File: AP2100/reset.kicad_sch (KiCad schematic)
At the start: 111 parts, among them IC4 MIC2774N-29YM5-TR, IC5 PCF2129T_2,518, J3 Conn_ARM_JTAG_SWD_10, J4 RJ45, SW1 RESET, U10 SA56004EDP,118, U11 SP3232EBEY-L/TR, U12 74LVC1G08, U13 74LVC1G08, U14 74LVC1G07, U15 74LVC1G07, U16 74LVC1G08, U17 74LVC1G07, U18 ATECC608A-MAHDA, U19 74LVC1G08, U20 74LVC1G07, U7 LS1043ASE7KQB-Layerscape, U9 74LVC2G08

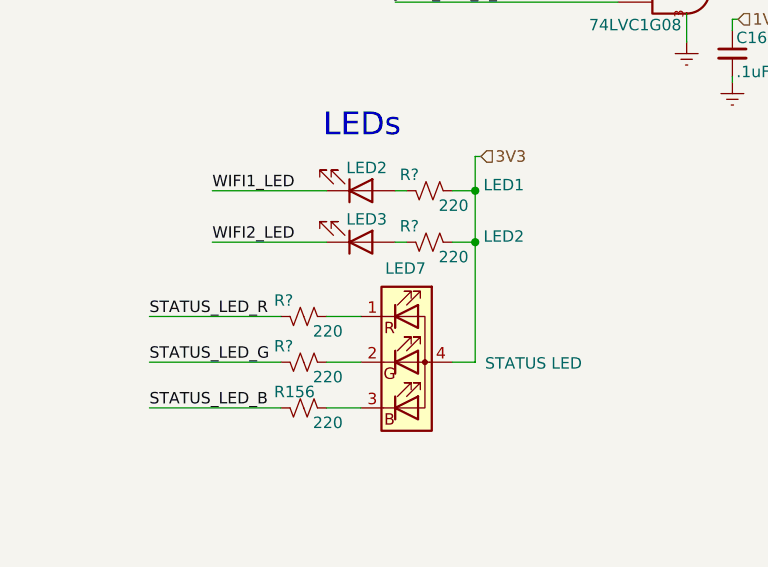
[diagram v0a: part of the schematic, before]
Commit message: Added antenna mounting holes
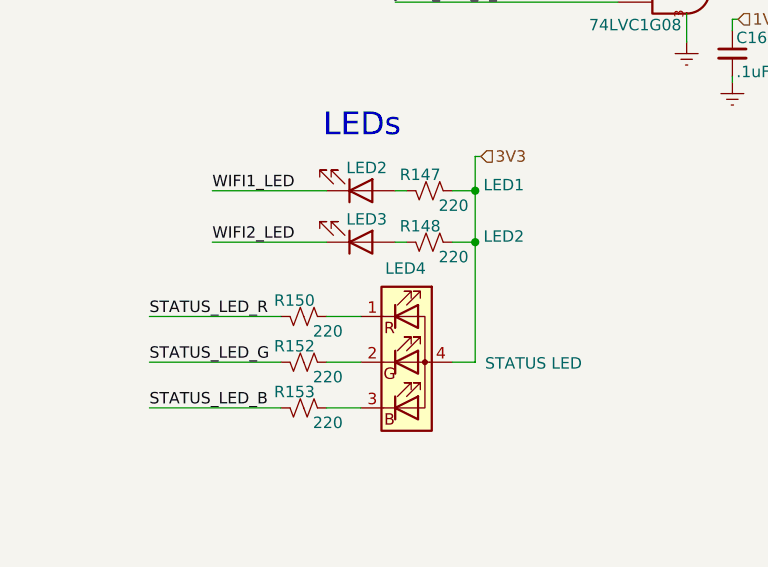
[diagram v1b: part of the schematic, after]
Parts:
- gave numbers to parts that had none: 4
- renumbered LED7 to LED4, R156 to R153
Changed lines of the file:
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@@
   (symbol (lib_id "Device:R_Small_US") (at 43.815 241.935 270) (mirror x) (unit 1)
     (in_bom yes) (on_board yes)
-    (property "Reference" "R?" (id 0) (at 40.513 240.157 90)
+    (property "Reference" "R150" (id 0) (at 40.513 240.157 90)
       (effects (font (size 1.27 1.27)) (justify left))
     )
@@
   (symbol (lib_id "Device:R_Small_US") (at 43.815 247.015 270) (mirror x) (unit 1)
     (in_bom yes) (on_board yes)
-    (property "Reference" "R?" (id 0) (at 40.513 245.237 90)
+    (property "Reference" "R152" (id 0) (at 40.513 245.237 90)
       (effects (font (size 1.27 1.27)) (justify left))
     )
@@
   (symbol (lib_id "Device:R_Small_US") (at 43.815 252.095 270) (mirror x) (unit 1)
     (in_bom yes) (on_board yes)
-    (property "Reference" "R156" (id 0) (at 40.513 250.317 90)
+    (property "Reference" "R153" (id 0) (at 40.513 250.317 90)
       (effects (font (size 1.27 1.27)) (justify left))
     )
@@
   (symbol (lib_id "Device:R_Small_US") (at 57.785 227.965 270) (mirror x) (unit 1)
     (in_bom yes) (on_board yes)
-    (property "Reference" "R?" (id 0) (at 54.483 226.187 90)
+    (property "Reference" "R147" (id 0) (at 54.483 226.187 90)
       (effects (font (size 1.27 1.27)) (justify left))
     )
@@
   (symbol (lib_id "Device:R_Small_US") (at 57.785 233.68 270) (mirror x) (unit 1)
     (in_bom yes) (on_board yes)
-    (property "Reference" "R?" (id 0) (at 54.483 231.902 90)
+    (property "Reference" "R148" (id 0) (at 54.483 231.902 90)
       (effects (font (size 1.27 1.27)) (justify left))
     )
@@
   (symbol (lib_id "Device:LED_RGBA") (at 55.245 247.015 0) (unit 1)
     (in_bom yes) (on_board yes)
-    (property "Reference" "LED7" (id 0) (at 55.118 236.601 0))
+    (property "Reference" "LED4" (id 0) (at 55.118 236.601 0))
     (property "Value" "STATUS LED" (id 1) (at 69.342 247.142 0))
     (property "Footprint" "LED_SMD:LED_Cree-PLCC4_2x2mm_CW" (id 2) (at 55.245 248.285 0)

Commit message: More cleanups
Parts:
- added R102, R103: 1K, Resistor_SMD:R_0402_1005Metric, symbol Device:R_Small_US
- added R110: 4.7K, Resistor_SMD:R_0402_1005Metric, symbol Device:R_Small_US
- R108: renamed from R105; value 1K -> 4.7K; PartsBoxID 0402-1K-1% -> 0402-4.7K-1%
- renumbered R134 to R100, R133 to R101, R101 to R104, R102 to R105, R103 to R106, R104 to R107, R106 to R109, R107 to R111, R108 to R112, R109 to R113, R110 to R114, R111 to R115, R112 to R116, R113 to R117, R114 to R118, R115 to R119, R116 to R120, R117 to R121, R118 to R122, R119 to R123, R120 to R124, R121 to R125, R122 to R126, R123 to R127, R124 to R128, R125 to R129, R126 to R130, R127 to R131, R128 to R132, R129 to R133, R130 to R134, R131 to R135, R132 to R136, R135 to R137, R136 to R138, R137 to R139, R138 to R140, R139 to R141, R140 to R142, R141 to R143, R142 to R144, R143 to R145, R144 to R146, R145 to R147, R146 to R148, R147 to R149, R148 to R150, R149 to R151, R150 to R152, R151 to R153, R152 to R154, R153 to R155, R89 to R88, R90 to R89, R91 to R90, R92 to R91, R93 to R92, R94 to R93, R95 to R94, R96 to R95, R97 to R96, R98 to R97, R99 to R98, R100 to R99
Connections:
- net 3V3: now also R102.2, R103.2
- net I2C1_SCL: now also R101.1
- net I2C1_SDA: now also R100.1
- net I2C2_SCL: now also R103.1
- net I2C2_SDA: now also R102.1
- net VDD_LP: now also R110.1; no longer U7.G19 (~TA_BB_TMP_DETECT~)
- net at IC5.4 (SDA/~CE), R142.2: no longer R100.1
- net at IC5.1 (SCL), R139.2: no longer R101.1
- new net: R110.2, U7.G19 (~TA_BB_TMP_DETECT~)
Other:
- moved on the sheet: C149, C151, R100, R101, R104, R105, R106, R107, R109, R111, R112, R113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

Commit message: Not sure
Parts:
- IC5: PartsBoxID (none) -> PCF2129T_2,518
- U10: PartsBoxID (none) -> SA56004EDP,118
- U11: value SP3232EBEY-L/TR -> SP3232EBEY-L/TR; PartsBoxID (none) -> SP3232EBEY-L/TR
- U12, U13, U16, U19: PartsBoxID (none) -> 74LVC1G08
- U14, U15, U17, U20: PartsBoxID (none) -> 74LVC1G07
- U18: PartsBoxID (none) -> ATECC608A-MAHDA
- U7: value LS1043ASE7KQB-Layerscape -> LS1043ASE7xxx; PartsBoxID (none) -> LS1043ASE7
- U9: PartsBoxID (none) -> 74LVC2G08
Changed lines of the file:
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@@
   (junction (at 376.555 177.8) (diameter 0.9144) (color 0 0 0 0))
   (no_connect (at 106.68 109.22))
-  (no_connect (at 238.76 71.12))
   (no_connect (at 217.805 177.165))
+  (no_connect (at 217.805 184.785))
   (no_connect (at 238.76 55.88))
+  (no_connect (at 238.76 71.12))
   (no_connect (at 250.825 179.705))
-  (no_connect (at 217.805 184.785))
   (wire (pts (xy 26.67 241.935) (xy 41.275 241.935))
     (stroke (width 0) (type solid) (color 0 0 0 0))
@@
     (stroke (width 0) (type solid) (color 0 0 0 0))
   )
-  (wire (pts (xy 317.5 57.15) (xy 317.5 59.69))
-    (stroke (width 0) (type solid) (color 0 0 0 0))
-  )
-  (wire (pts (xy 317.5 59.69) (xy 317.5 60.325))
+  (wire (pts (xy 317.5 57.15) (xy 317.5 60.325))
     (stroke (width 0) (type solid) (color 0 0 0 0))
   )
@@
     (stroke (width 0) (type solid) (color 0 0 0 0))
   )
-  (wire (pts (xy 340.995 57.15) (xy 340.995 59.69))
-    (stroke (width 0) (type solid) (color 0 0 0 0))
-  )
-  (wire (pts (xy 340.995 59.69) (xy 340.995 60.325))
+  (wire (pts (xy 340.995 57.15) (xy 340.995 60.325))
     (stroke (width 0) (type solid) (color 0 0 0 0))
   )
@@
       (effects (font (size 1.27 1.27)) hide)
     )
+    (property "PartsBoxID" "74LVC2G08" (id 4) (at 72.39 43.18 0)
+      (effects (font (size 1.27 1.27)) hide)
+    )
   )
   (symbol (lib_name "Scott:74LVC1G08_2") (lib_id "Scott:74LVC1G08") (at 86.36 205.74 0) (unit 1)
@@
       (effects (font (size 1.27 1.27)) hide)
     )
+    (property "PartsBoxID" "74LVC1G08" (id 4) (at 86.36 205.74 0)
+      (effects (font (size 1.27 1.27)) hide)
+    )
   )
   (symbol (lib_name "Scott:74LVC1G08_1") (lib_id "Scott:74LVC1G08") (at 101.6 189.865 0) (unit 1)
@@
       (effects (font (size 1.27 1.27)) hide)
     )
+    (property "PartsBoxID" "74LVC1G08" (id 4) (at 101.6 189.865 0)
+      (effects (font (size 1.27 1.27)) hide)
+    )
   )
   (symbol (lib_name "Scott:74LVC1G07_1") (lib_id "Scott:74LVC1G07") (at 146.05 205.74 0) (unit 1)
@@
       (effects (font (size 1.27 1.27)) hide)
     )
+    (property "PartsBoxID" "74LVC1G07" (id 4) (at 146.05 205.74 0)
+      (effects (font (size 1.27 1.27)) hide)
+    )
   )
   (symbol (lib_name "Scott:74LVC1G07_2") (lib_id "Scott:74LVC1G07") (at 146.05 220.98 0) (unit 1)
@@
       (effects (font (size 1.27 1.27)) hide)
     )
+    (property "PartsBoxID" "74LVC1G07" (id 4) (at 146.05 220.98 0)
+      (effects (font (size 1.27 1.27)) hide)
+    )
   )
   (symbol (lib_name "Scott:74LVC1G08_3") (lib_id "Scott:74LVC1G08") (at 150.495 239.395 0) (unit 1)
@@
       (effects (font (size 1.27 1.27)) hide)
     )
+    (property "PartsBoxID" "74LVC1G08" (id 4) (at 150.495 239.395 0)
+      (effects (font (size 1.27 1.27)) hide)
+    )
   )
   (symbol (lib_id "Scott:74LVC1G08") (at 150.495 259.08 0) (unit 1)
@@
       (effects (font (size 1.27 1.27)) hide)
     )
+    (property "PartsBoxID" "74LVC1G08" (id 4) (at 150.495 259.08 0)
+      (effects (font (size 1.27 1.27)) hide)
+    )
   )
   (symbol (lib_name "Scott:74LVC1G07_3") (lib_id "Scott:74LVC1G07") (at 174.625 239.395 0) (unit 1)
@@
       (effects (font (size 1.27 1.27)) hide)
     )
+    (property "PartsBoxID" "74LVC1G07" (id 4) (at 174.625 239.395 0)
+      (effects (font (size 1.27 1.27)) hide)
+    )
   )
   (symbol (lib_id "Scott:74LVC1G07") (at 174.625 259.08 0) (unit 1)
@@
       (effects (font (size 1.27 1.27)) hide)
     )
+    (property "PartsBoxID" "74LVC1G07" (id 4) (at 174.625 259.08 0)
+      (effects (font (size 1.27 1.27)) hide)
+    )
   )
   (symbol (lib_id "Scott:74LVC2G08") (at 328.295 97.79 0) (unit 2)
@@
       (effects (font (size 1.27 1.27)) hide)
     )
+    (property "PartsBoxID" "74LVC2G08" (id 4) (at 328.295 97.79 0)
+      (effects (font (size 1.27 1.27)) hide)
+    )
   )
   (symbol (lib_id "Device:LED_RGBA") (at 55.245 247.015 0) (unit 1)
@@
       (effects (font (size 1.27 1.27)) hide)
     )
+    (property "PartsBoxID" "ATECC608A-MAHDA" (id 4) (at 259.08 239.395 0)
+      (effects (font (size 1.27 1.27)) hide)
+    )
   )
   (symbol (lib_id "MIC2774L-29YM5-TR:MIC2774L-29YM5-TR") (at 135.89 164.465 0) (mirror y) (unit 1)
@@
       (effects (font (size 1.27 1.27)) (justify left bottom) hide)
     )
+    (property "PartsBoxID" "SA56004EDP,118" (id 4) (at 283.845 96.52 0)
+      (effects (font (size 1.27 1.27)) hide)
+    )
   )
   (symbol (lib_id "Connector:RJ45") (at 389.89 175.26 180) (unit 1)
@@
       (effects (font (size 1.27 1.27)) (justify left) hide)
     )
+    (property "PartsBoxID" "PCF2129T_2,518" (id 4) (at 217.805 172.085 0)
+      (effects (font (size 1.27 1.27)) hide)
+    )
   )
   (symbol (lib_id "Interface_UART:MAX3232") (at 330.835 165.1 0) (unit 1)
     (in_bom yes) (on_board yes)
     (property "Reference" "U11" (id 0) (at 316.865 137.795 0))
-    (property "Value" "SP3232EBEY-L/TR\n" (id 1) (at 320.04 191.77 0))
+    (property "Value" "SP3232EBEY-L/TR" (id 1) (at 320.04 191.77 0))
     (property "Footprint" "Package_SO:TSSOP-16_4.4x5mm_P0.65mm" (id 2) (at 332.105 191.77 0)
       (effects (font (size 1.27 1.27)) (justify left) hide)
@@
       (effects (font (size 1.27 1.27)) hide)
     )
+    (property "PartsBoxID" "SP3232EBEY-L/TR" (id 4) (at 330.835 165.1 0)
+      (effects (font (size 1.27 1.27)) hide)
+    )
   )
   (symbol (lib_id "AP2100-rescue:LS1043ASE7KQB-Layerscape") (at 171.45 80.01 0) (unit 5)
     (in_bom yes) (on_board yes)
     (property "Reference" "U7" (id 0) (at 173.355 25.4 0))
-    (property "Value" "LS1043ASE7KQB-Layerscape" (id 1) (at 173.355 27.94 0))
+    (property "Value" "LS1043ASE7xxx" (id 1) (at 173.355 27.94 0))
     (property "Footprint" "PLS1043ASE7QQA:BGA621C80P25X25_2100X2100X192N" (id 2) (at 171.45 80.01 0)
       (effects (font (size 1.27 1.27)) hide)
@@
       (effects (font (size 1.27 1.27)) hide)
     )
+    (property "PartsBoxID" "LS1043ASE7" (id 4) (at 171.45 80.01 0)
+      (effects (font (size 1.27 1.27)) hide)
+    )

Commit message: More cleanups - fix incorrect serial console pinout Add netclasses
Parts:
- removed R88, R90, R95, R97: DNP 0, Resistor_SMD:R_0402_1005Metric, symbol Device:R_Small_US
- removed R89, R91, R96, R98: 0, Resistor_SMD:R_0402_1005Metric, symbol Device:R_Small_US
- renumbered R108 to R100, R109 to R101, R110 to R102, R111 to R103, R112 to R104, R113 to R105, R114 to R106, R115 to R107, R116 to R108, R117 to R109, R118 to R110, R119 to R111, R120 to R112, R121 to R113, R122 to R114, R123 to R115, R124 to R116, R125 to R117, R126 to R118, R127 to R119, R128 to R120, R129 to R121, R130 to R122, R131 to R123, R132 to R124, R133 to R125, R134 to R126, R135 to R127, R136 to R128, R137 to R129, R138 to R130, R139 to R131, R141 to R132, R140 to R133, R142 to R134, R143 to R135, R144 to R136, R145 to R137, R146 to R138, R147 to R139, R148 to R140, R149 to R141, R150 to R142, R151 to R143, R152 to R144, R153 to R145, R154 to R146, R155 to R147, R92 to R88, R93 to R89, R94 to R90, R99 to R91, R100 to R92, R101 to R93, R102 to R94, R103 to R95, R104 to R96, R105 to R97, R106 to R98, R107 to R99
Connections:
- net CONSOLE_CTS is gone; now on net UART_RTS: U11.10 (T2IN)
- net CONSOLE_RTS is gone; now on net UART_CTS: U11.9 (R2OUT)
- net CONSOLE_RX is gone; now on net UART_RX: U11.12 (R1OUT)
- net CONSOLE_TX is gone; now on net UART_TX: U11.11 (T1IN)
- net at J4.1: now also U11.7 (T2OUT); no longer U11.8 (R2IN)
- net at J4.8: now also U11.8 (R2IN); no longer U11.7 (T2OUT)
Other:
- note added: "Note: I2C Address: 0x4C"
- note added: "Note: I2C Address: 0x51"
- note added: "Note: I2C Address: 0x60"
- company: (none) -> ISis ImageStream Internet Solutions, Inc.
- title: (none) -> AP2100
- moved on the sheet: BT1, C149, C150, C151, C152, C153, C154, C155, C156, C157, C158, C159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

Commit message: More cleanups
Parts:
- BT1: PartsBoxID (none) -> 2032-BH
- LED6: renamed from LED1; PartsBoxID (none) -> 0805-LED-BLUE
- LED7: renamed from LED2; value LED1 -> WIFI1_LED; PartsBoxID (none) -> 0805-LED-GREEN
- LED8: renamed from LED3; value LED2 -> WIFI2_LED; PartsBoxID (none) -> 0805-LED-GREEN
- LED9: renamed from LED4; PartsBoxID (none) -> 2x2-LED-RGB
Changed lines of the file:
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@@
   (junction (at 69.85 111.125) (diameter 0.9144) (color 0 0 0 0))
   (junction (at 74.295 52.705) (diameter 0.9144) (color 0 0 0 0))
+  (junction (at 74.295 159.385) (diameter 0.9144) (color 0 0 0 0))
   (junction (at 75.565 116.205) (diameter 0.9144) (color 0 0 0 0))
-  (junction (at 76.2 159.385) (diameter 0.9144) (color 0 0 0 0))
   (junction (at 92.075 168.275) (diameter 0.9144) (color 0 0 0 0))
   (junction (at 92.075 182.88) (diameter 0.9144) (color 0 0 0 0))
@@
   (junction (at 365.76 154.305) (diameter 0.9144) (color 0 0 0 0))
   (junction (at 381.635 167.005) (diameter 0.9144) (color 0 0 0 0))
-  (no_connect (at 223.52 168.91))
-  (no_connect (at 223.52 176.53))
-  (no_connect (at 244.475 47.625))
   (no_connect (at 244.475 62.865))
+  (no_connect (at 244.475 47.625))
+  (no_connect (at 223.52 176.53))
+  (no_connect (at 223.52 168.91))
   (no_connect (at 112.395 100.965))
   (no_connect (at 256.54 171.45))
@@
     (stroke (width 0) (type solid) (color 0 0 0 0))
   )
-  (wire (pts (xy 73.66 149.86) (xy 78.74 149.86))
+  (wire (pts (xy 71.755 149.86) (xy 78.74 149.86))
     (stroke (width 0) (type solid) (color 0 0 0 0))
   )
-  (wire (pts (xy 73.66 153.035) (xy 78.74 153.035))
+  (wire (pts (xy 71.755 153.035) (xy 78.74 153.035))
     (stroke (width 0) (type solid) (color 0 0 0 0))
   )
-  (wire (pts (xy 73.66 156.21) (xy 78.74 156.21))
+  (wire (pts (xy 71.755 156.21) (xy 78.74 156.21))
     (stroke (width 0) (type solid) (color 0 0 0 0))
   )
-  (wire (pts (xy 73.66 159.385) (xy 76.2 159.385))
+  (wire (pts (xy 71.755 159.385) (xy 74.295 159.385))
     (stroke (width 0) (type solid) (color 0 0 0 0))
   )
@@
     (stroke (width 0) (type solid) (color 0 0 0 0))
   )
-  (wire (pts (xy 75.565 100.965) (xy 75.565 102.235))
+  (wire (pts (xy 74.295 159.385) (xy 74.295 196.215))
     (stroke (width 0) (type solid) (color 0 0 0 0))
   )
-  (wire (pts (xy 75.565 116.205) (xy 75.565 107.315))
+  (wire (pts (xy 74.295 159.385) (xy 78.74 159.385))
     (stroke (width 0) (type solid) (color 0 0 0 0))
   )
-  (wire (pts (xy 75.565 116.205) (xy 112.395 116.205))
+  (wire (pts (xy 74.295 196.215) (xy 77.47 196.215))
     (stroke (width 0) (type solid) (color 0 0 0 0))
   )
-  (wire (pts (xy 76.2 27.94) (xy 78.105 27.94))
+  (wire (pts (xy 75.565 100.965) (xy 75.565 102.235))
     (stroke (width 0) (type solid) (color 0 0 0 0))
   )
-  (wire (pts (xy 76.2 159.385) (xy 76.2 196.215))
+  (wire (pts (xy 75.565 116.205) (xy 75.565 107.315))
     (stroke (width 0) (type solid) (color 0 0 0 0))
   )
-  (wire (pts (xy 76.2 159.385) (xy 78.74 159.385))
+  (wire (pts (xy 75.565 116.205) (xy 112.395 116.205))
     (stroke (width 0) (type solid) (color 0 0 0 0))
   )
-  (wire (pts (xy 76.2 196.215) (xy 77.47 196.215))
+  (wire (pts (xy 76.2 27.94) (xy 78.105 27.94))
     (stroke (width 0) (type solid) (color 0 0 0 0))
   )
@@
     (effects (font (size 1.27 1.27)) (justify left))
   )
-  (hierarchical_label "CPU_VDD_PG" (shape input) (at 73.66 149.86 180)
+  (hierarchical_label "CPU_VDD_PG" (shape input) (at 71.755 149.86 180)
     (effects (font (size 1.27 1.27)) (justify right))
   )
-  (hierarchical_label "3V3_PG" (shape input) (at 73.66 153.035 180)
+  (hierarchical_label "3V3_PG" (shape input) (at 71.755 153.035 180)
     (effects (font (size 1.27 1.27)) (justify right))
   )
-  (hierarchical_label "5V_PG" (shape input) (at 73.66 156.21 180)
+  (hierarchical_label "5V_PG" (shape input) (at 71.755 156.21 180)
     (effects (font (size 1.27 1.27)) (justify right))
   )
-  (hierarchical_label "PMIC_POR_B" (shape input) (at 73.66 159.385 180)
+  (hierarchical_label "PMIC_POR_B" (shape input) (at 71.755 159.385 180)
     (effects (font (size 1.27 1.27)) (justify right))
   )
@@
   (symbol (lib_id "Device:LED") (at 55.88 219.71 0) (mirror x) (unit 1)
     (in_bom yes) (on_board yes)
-    (property "Reference" "LED2" (id 0) (at 56.515 217.17 0))
-    (property "Value" "LED1" (id 1) (at 71.755 219.075 0))
+    (property "Reference" "LED7" (id 0) (at 56.515 217.17 0))
+    (property "Value" "WIFI1_LED" (id 1) (at 74.295 219.075 0))
     (property "Footprint" "LED_SMD:LED_0805_2012Metric" (id 2) (at 55.88 219.71 0)
       (effects (font (size 1.27 1.27)) hide)
@@
       (effects (font (size 1.27 1.27)) hide)
     )
+    (property "PartsBoxID" "0805-LED-GREEN" (id 4) (at 55.88 219.71 0)
+      (effects (font (size 1.27 1.27)) hide)
+    )
   )
   (symbol (lib_id "Device:LED") (at 55.88 225.425 0) (mirror x) (unit 1)
     (in_bom yes) (on_board yes)
-    (property "Reference" "LED3" (id 0) (at 56.515 222.885 0))
-    (property "Value" "LED2" (id 1) (at 71.755 224.79 0))
+    (property "Reference" "LED8" (id 0) (at 56.515 222.885 0))
+    (property "Value" "WIFI2_LED" (id 1) (at 74.295 224.79 0))
     (property "Footprint" "LED_SMD:LED_0805_2012Metric" (id 2) (at 55.88 225.425 0)
       (effects (font (size 1.27 1.27)) hide)
@@
       (effects (font (size 1.27 1.27)) hide)
     )
+    (property "PartsBoxID" "0805-LED-GREEN" (id 4) (at 55.88 225.425 0)
+      (effects (font (size 1.27 1.27)) hide)
+    )
   )
   (symbol (lib_id "Device:LED") (at 130.175 181.61 180) (unit 1)
     (in_bom yes) (on_board yes)
-    (property "Reference" "LED1" (id 0) (at 129.54 178.435 0))
+    (property "Reference" "LED6" (id 0) (at 129.54 178.435 0))
     (property "Value" "PWRLED" (id 1) (at 143.51 182.245 0)
       (effects (font (size 2.032 2.032)))
@@
       (effects (font (size 1.27 1.27)) hide)
     )
+    (property "PartsBoxID" "0805-LED-BLUE" (id 4) (at 130.175 181.61 0)
+      (effects (font (size 1.27 1.27)) hide)
+    )
   )
   (symbol (lib_id "Switch:SW_SPST") (at 270.51 50.165 0) (unit 1)
@@
       (effects (font (size 1.27 1.27)) hide)
     )
+    (property "PartsBoxID" "2032-BH" (id 4) (at 281.305 172.72 0)
+      (effects (font (size 1.27 1.27)) hide)
+    )
   )
   (symbol (lib_name "Scott:74LVC2G08_1") (lib_id "Scott:74LVC2G08") (at 78.105 34.925 0) (unit 1)
@@
   (symbol (lib_id "Device:LED_RGBA") (at 60.96 238.76 0) (unit 1)
     (in_bom yes) (on_board yes)
-    (property "Reference" "LED4" (id 0) (at 60.833 228.346 0))
+    (property "Reference" "LED9" (id 0) (at 60.833 228.346 0))
     (property "Value" "STATUS LED" (id 1) (at 75.057 238.887 0))
     (property "Footprint" "LED_SMD:LED_Cree-PLCC4_2x2mm_CW" (id 2) (at 60.96 240.03 0)
@@
       (effects (font (size 1.27 1.27)) hide)
     )
+    (property "PartsBoxID" "2x2-LED-RGB" (id 4) (at 60.96 238.76 0)
+      (effects (font (size 1.27 1.27)) hide)
+    )
